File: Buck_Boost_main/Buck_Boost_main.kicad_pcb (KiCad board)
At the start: 2 copper layers, 0 parts

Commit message: NEW COMMENT RAHHHHHH
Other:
- board text added: "Test1234"
- board text removed: "Test123"
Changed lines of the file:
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@@
 	)
 	(net 0 "")
-	(gr_text "Test123"
+	(gr_text "Test1234"
 		(at 23.89 23.37 0)
 		(layer "F.Cu")

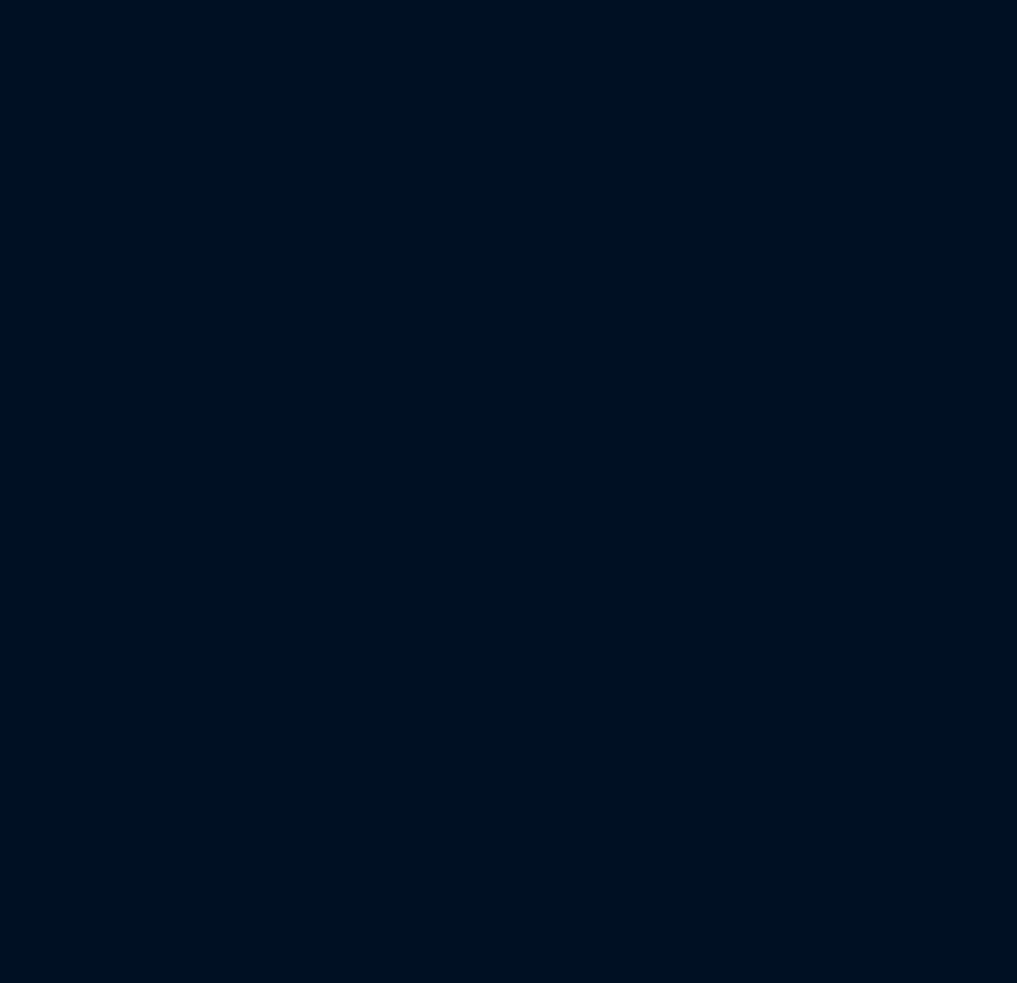
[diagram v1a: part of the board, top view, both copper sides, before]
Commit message: Placed in Inductor, Controller, and Fets, along with obligatory heatsink, screw terms, and fuses.
I realized that we already have an extra 15uh power inductor from the bucks with very low dcr and high sat current (1.62mohm, 16A), so we can use this one:(PQ2614BHA-150K)
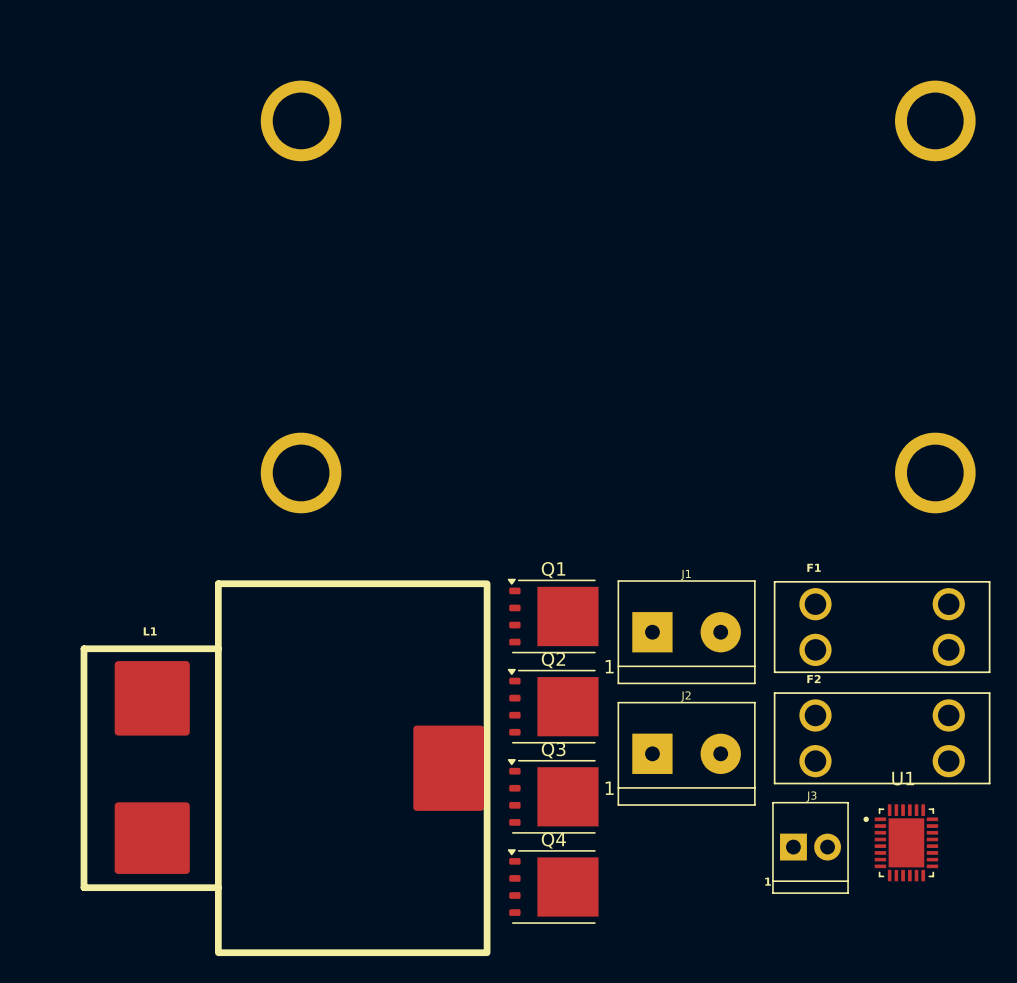
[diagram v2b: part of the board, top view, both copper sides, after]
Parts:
- added F1: Fuse_Holder_Auto, rsx_fuses:FUSE_3568-10, F.Cu at (174.9, 99.5)
- added F2: Fuse_Holder_Auto, rsx_fuses:FUSE_3568-10, F.Cu at (174.9, 107.8)
- added HW1: Board_Mount_Heat_Sink_Screw_2.5C/W, rsx_misc:ATS-1139-C1-R0, B.Cu at (155.3, 74.9)
- added J1: Screw_Terminal_2x5.08, rsx_headers_screw:Molex_0398800302, F.Cu at (157.8, 99.9)
- added J2: Screw_Terminal_2x5.08, rsx_headers_screw:Molex_0398800302, F.Cu at (157.8, 108.9)
- added J3: Screw_Terminal_2x2.54, rsx_headers_screw:Wurth_691210910002, F.Cu at (169.1, 115.9)
- added L1: 15u, rsx_inductors:PQ2617BHA-XXXK, F.Cu at (130.6, 110.0)
- added Q1: CSD18532Q5B, Package_TO_SOT_SMD:TDSON-8-1, F.Cu at (150.5, 98.7)
- added Q2: CSD18532Q5B, Package_TO_SOT_SMD:TDSON-8-1, F.Cu at (150.5, 105.4)
- added Q3: CSD18532Q5B, Package_TO_SOT_SMD:TDSON-8-1, F.Cu at (150.5, 112.1)
- added Q4: CSD18532Q5B, Package_TO_SOT_SMD:TDSON-8-1, F.Cu at (150.5, 118.8)
- added U1: LT8390EUFD_PBF, LT:QFN50P500X400X80-29N, F.Cu at (176.7, 115.5)
